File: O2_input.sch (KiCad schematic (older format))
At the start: 2 parts, among them P18 CONN_1, P19 CONN_1

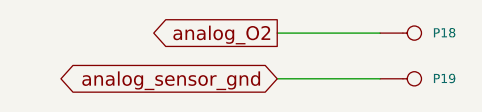
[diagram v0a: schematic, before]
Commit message: DFH mans up a bit. Perhaps usable for something at this point, like making trips to the local store ;)
I connected TA pins to sub circuits, fixed a number if items discussed in the DIYEFI forums. This is it's 21st version, so it was time for it to man up a bit, and become something potentially useful.

Signed-off-by: Jared Harvey <TortiseGIT@jaredharvey.com>
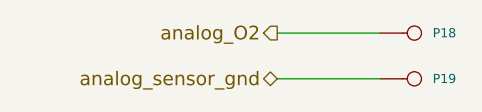
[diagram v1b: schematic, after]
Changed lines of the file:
@@
-EESchema Schematic File Version 1
-LIBS:power,./freeEMS_lib,device,conn,linear,regul,74xx,cmos4000,adc-dac,memory,xilinx,special,microcontrollers,dsp,microchip,analog_switches,motorola,texas,intel,audio,interface,digital-audio,philips,display,cypress,siliconi,contrib,valves,./freeEMS_1.cache
-EELAYER 23  0
+EESchema Schematic File Version 2  date 9/10/2011 11:43:51 AM
+LIBS:power
+LIBS:freeEMS_lib
+LIBS:device
+LIBS:conn
+LIBS:linear
+LIBS:regul
+LIBS:74xx
+LIBS:cmos4000
+LIBS:adc-dac
+LIBS:memory
+LIBS:xilinx
+LIBS:special
+LIBS:microcontrollers
+LIBS:dsp
+LIBS:microchip
+LIBS:analog_switches
+LIBS:motorola
+LIBS:texas
+LIBS:intel
+LIBS:audio
+LIBS:interface
+LIBS:digital-audio
+LIBS:philips
+LIBS:display
+LIBS:cypress
+LIBS:siliconi
+LIBS:contrib
+LIBS:valves
+LIBS:freeEMS_1-cache
+EELAYER 25  0
 EELAYER END
 $Descr A4 11700 8267
+encoding utf-8
 Sheet 24 41
-Title "freeEMS 1.0"
-Date "15 nov 2008"
-Rev "A.20"
-Comp "diyefi.org"
+Title "DFH for freeEMS"
+Date "10 sep 2011"
+Rev "A.21"
+Comp "FreeEMS.org"
 Comment1 "O2_input.sch"
 Comment2 ""
@@
 U 1 1 48AA1A98
 P 3200 2500
-F 0 "P19" H 3280 2500 40  0000 L C
-F 1 "CONN_1" H 3200 2555 30  0001 C C
-F 2 "1PIN" V 1130 2600 60  0001 C C
+F 0 "P19" H 3280 2500 40  0000 L CNN
+F 1 "CONN_1" H 3200 2555 30  0001 C CNN
+F 2 "1PIN" V 1130 2600 60  0001 C CNN
 	1    3200 2500
 	1    0    0    -1
@@
 U 1 1 48AA1A96
 P 3200 2300
-F 0 "P18" H 3280 2300 40  0000 L C
-F 1 "CONN_1" H 3200 2355 30  0001 C C
-F 2 "1PIN" V 1130 2600 60  0001 C C
+F 0 "P18" H 3280 2300 40  0000 L CNN
+F 1 "CONN_1" H 3200 2355 30  0001 C CNN
+F 2 "1PIN" V 1130 2600 60  0001 C CNN
 	1    3200 2300
 	1    0    0    -1
@@
 Wire Wire Line
 	2600 2300 3050 2300
-Text GLabel 2600 2500 0    60   BiDi
+Text HLabel 2600 2500 0    60   BiDi ~ 0
 analog_sensor_gnd
-Text GLabel 2600 2300 0    60   Output
+Text HLabel 2600 2300 0    60   Output ~ 0
 analog_O2
 $EndSCHEMATC
